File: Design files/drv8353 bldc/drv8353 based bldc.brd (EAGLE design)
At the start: 127 x 127 mm, 117 parts, among them IC1 DRV8353RSRGZT, J3 2X6 FEMALE, J4 B06B-HCMKK

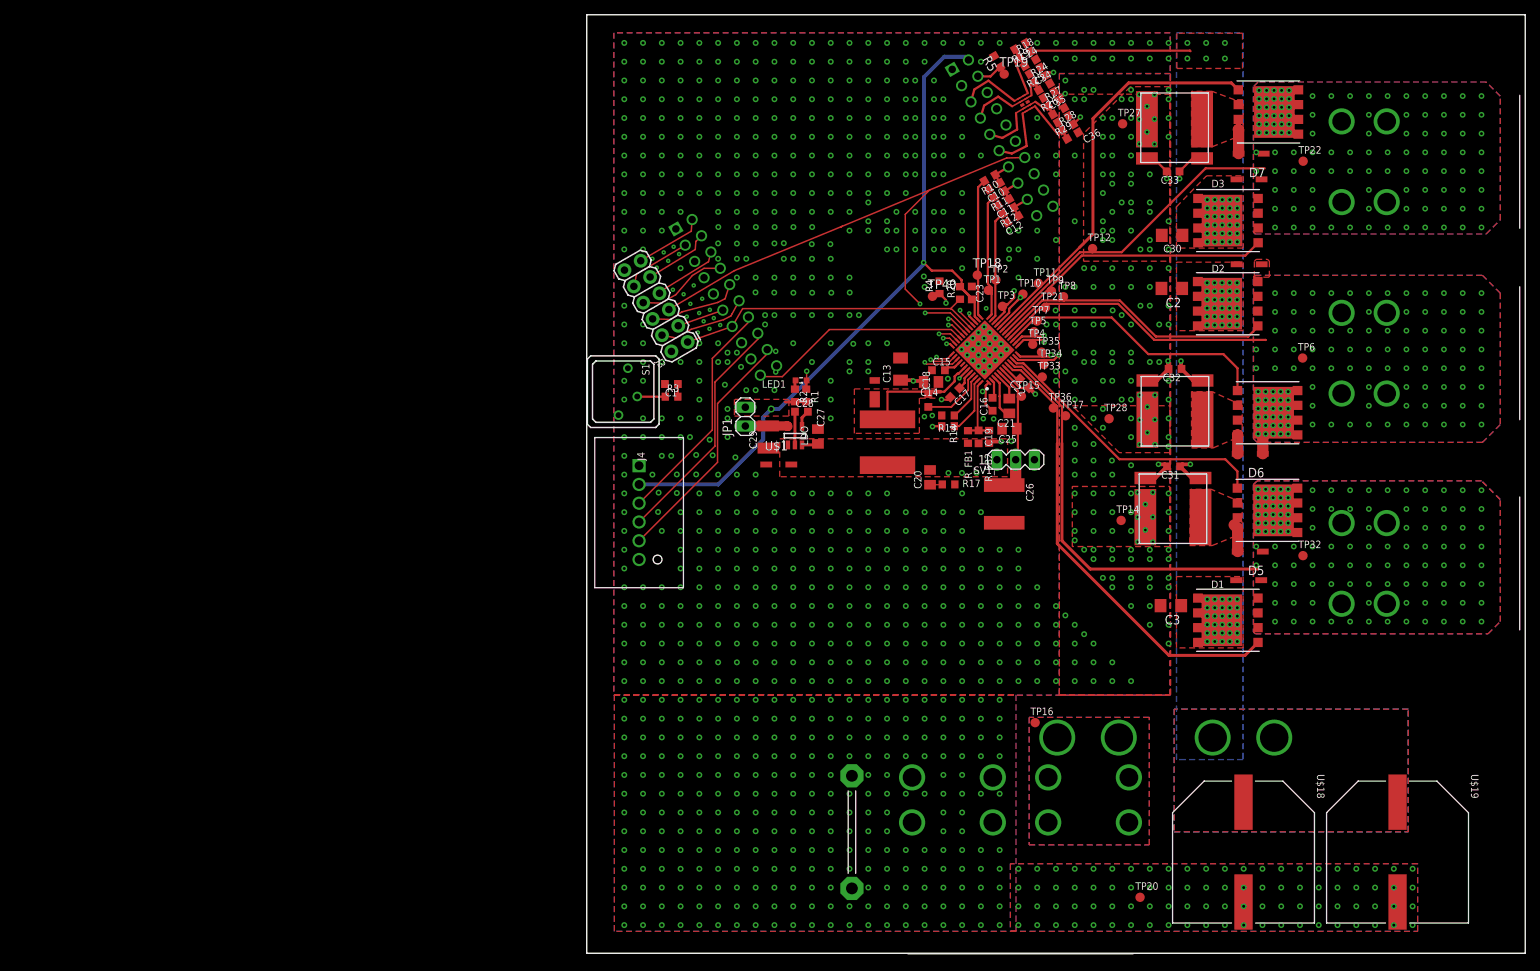
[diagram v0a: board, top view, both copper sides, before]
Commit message: silkscreen pass, slightly moved fuse to prevent part collision
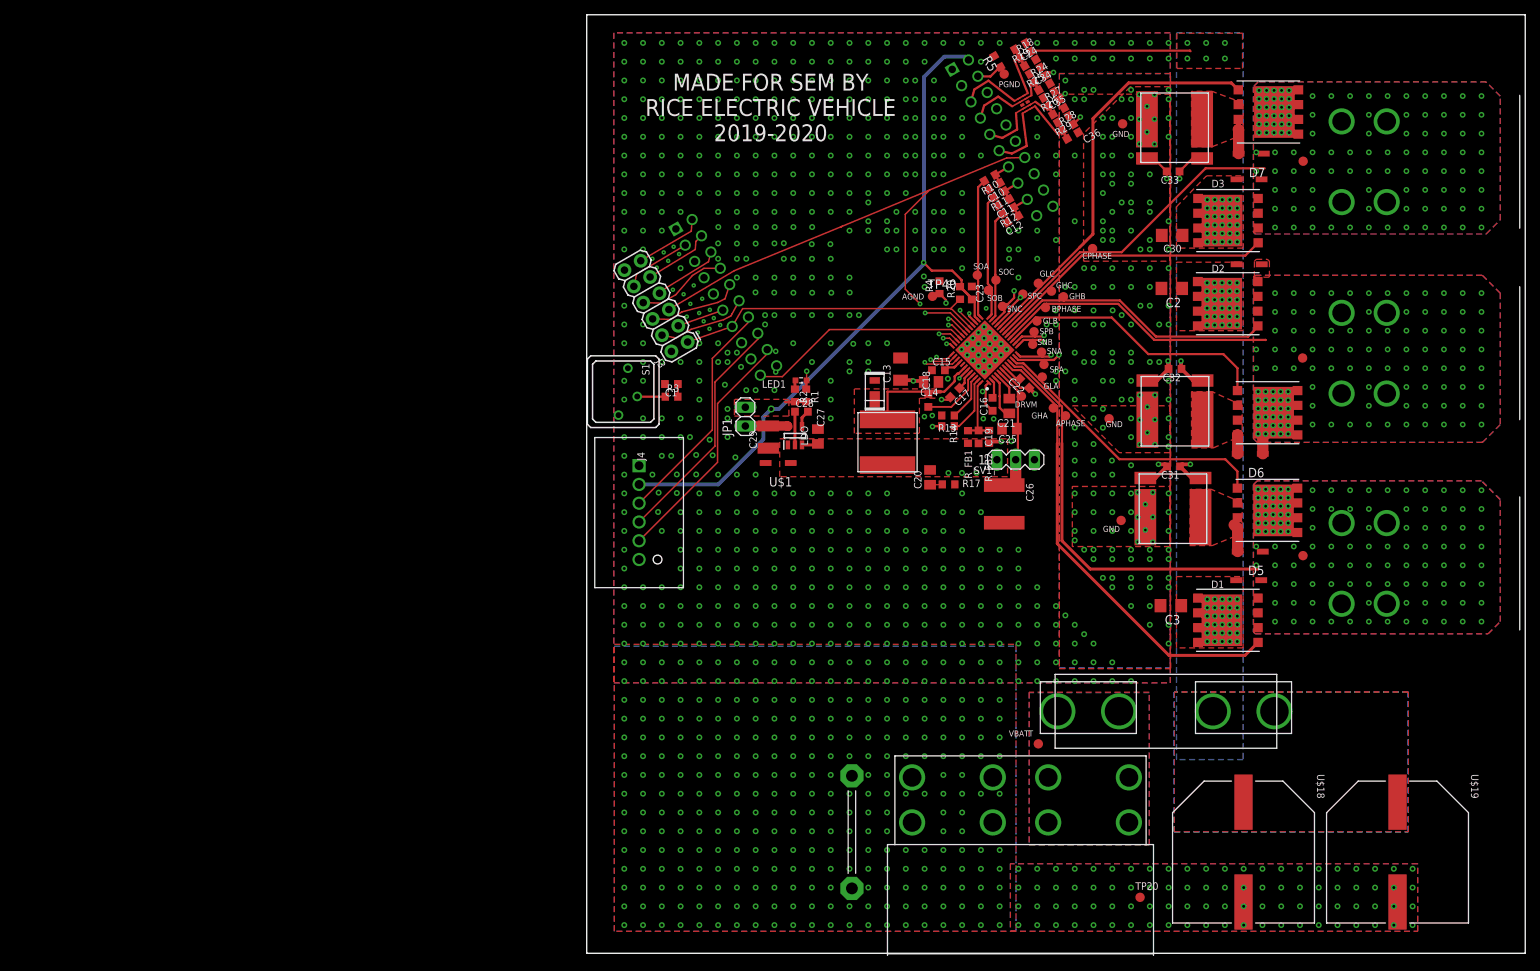
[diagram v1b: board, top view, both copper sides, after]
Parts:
- moved F1 3.56 mm to (78.4, 32.7)
- moved TP16 2.90 mm to (61.1, 28.3)
- moved U$1 0.22 mm to (25.9, 66.3), turned to 180 degrees
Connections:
- net APHASE: now also D5.LINE; no longer D5.1
- net BPHASE: now also D6.LINE; no longer D6.1
- net CPHASE: now also D7.LINE; no longer D7.1
- net GND: now also U$1.2; no longer U$1.1
- net VBUCK: now also U$1.LINE; no longer U$1.2
- net VDRAIN: now also D1.LINE, D2.LINE, D3.LINE; no longer D1.1, D2.1, D3.1
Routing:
- net VDRAIN: track 81.2 -> 78.2 mm
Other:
- board text added: "AGND"
- board text added: "APHASE"
- board text added: "BPHASE"
- board text added: "CPHASE"
- board text added: "DRVM"
- board text added: "GHA"
- board text added: "GHB"
- board text added: "GHC"
- board text added: "GLA"
- board text added: "GLB"
- board text added: "GLC"
- board text added: "GND"
- board text added: "MADE FOR SEM BY RICE ELECTRIC VEHICLE 2019-2020"
- board text added: "PGND"
- board text added: "SNA"
- board text added: "SNB"
- board text added: "SNC"
- board text added: "SOA"
- board text added: "SOB"
- board text added: "SOC"
- board text added: "SPA"
- board text added: "SPB"
- board text added: "SPC"
- board text added: "VBATT"

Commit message: corrected drc
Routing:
- net CPHASE: vias 111 -> 110
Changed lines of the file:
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@@
 <setting verticaltext="up"/>
 </settings>
-<grid distance="1" unitdist="mil" unit="mil" style="lines" multiple="1" display="no" altdistance="0.1" altunitdist="mil" altunit="mil"/>
+<grid distance="1" unitdist="mil" unit="mm" style="lines" multiple="1" display="no" altdistance="0.1" altunitdist="mil" altunit="mil"/>
 <layers>
 <layer number="1" name="Top" color="4" fill="1" visible="yes" active="yes"/>
@@
 <param name="mtCopper" value="0.035mm 0.0175mm 0.035mm 0.035mm 0.035mm 0.035mm 0.035mm 0.035mm 0.035mm 0.035mm 0.035mm 0.035mm 0.035mm 0.035mm 0.0175mm 0.035mm"/>
 <param name="mtIsolate" value="0.1mm 0.5mm 0.2mm 0.15mm 0.2mm 0.15mm 0.2mm 0.15mm 0.2mm 0.15mm 0.2mm 0.15mm 0.2mm 0.15mm 0.1mm"/>
-<param name="mdWireWire" value="6mil"/>
-<param name="mdWirePad" value="6mil"/>
-<param name="mdWireVia" value="6mil"/>
-<param name="mdPadPad" value="6mil"/>
-<param name="mdPadVia" value="6mil"/>
-<param name="mdViaVia" value="6mil"/>
+<param name="mdWireWire" value="0.2mm"/>
+<param name="mdWirePad" value="0.2mm"/>
+<param name="mdWireVia" value="0.2mm"/>
+<param name="mdPadPad" value="0.2mm"/>
+<param name="mdPadVia" value="0.2mm"/>
+<param name="mdViaVia" value="0.2mm"/>
 <param name="mdSmdPad" value="6mil"/>
 <param name="mdSmdVia" value="6mil"/>
@@
 <param name="mdDrill" value="6mil"/>
 <param name="mdSmdStop" value="0mil"/>
-<param name="msWidth" value="6mil"/>
-<param name="msDrill" value="10mil"/>
+<param name="msWidth" value="0.2mm"/>
+<param name="msDrill" value="0.2mm"/>
 <param name="msMicroVia" value="9.99mm"/>
 <param name="msBlindViaRatio" value="0.5"/>
@@
 <param name="rvMicroViaOuter" value="0.25"/>
 <param name="rvMicroViaInner" value="0.25"/>
-<param name="rlMinPadTop" value="10mil"/>
+<param name="rlMinPadTop" value="0.2mm"/>
 <param name="rlMaxPadTop" value="20mil"/>
-<param name="rlMinPadInner" value="10mil"/>
+<param name="rlMinPadInner" value="0.2mm"/>
 <param name="rlMaxPadInner" value="20mil"/>
-<param name="rlMinPadBottom" value="10mil"/>
+<param name="rlMinPadBottom" value="0.2mm"/>
 <param name="rlMaxPadBottom" value="20mil"/>
-<param name="rlMinViaOuter" value="8mil"/>
+<param name="rlMinViaOuter" value="0.2mm"/>
 <param name="rlMaxViaOuter" value="20mil"/>
-<param name="rlMinViaInner" value="8mil"/>
+<param name="rlMinViaInner" value="0.2mm"/>
 <param name="rlMaxViaInner" value="20mil"/>
 <param name="rlMinMicroViaOuter" value="4mil"/>
@@
 <wire x1="28.1758" y1="73.2824" x2="28.1796" y2="73.2862" width="0.4064" layer="1"/>
 <wire x1="24.5636" y1="68.3582" x2="24.6398" y2="68.3582" width="0.508" layer="1"/>
+<wire x1="51.4858" y1="80.9498" x2="50.86859375" y2="79.69425625" width="0" layer="19" extent="1-1"/>
+<wire x1="59.6695625" y1="115.21495" x2="60.96" y2="113.03" width="0" layer="19" extent="1-1"/>
+<wire x1="55.662825" y1="101.1909" x2="56.897225" y2="98.9091" width="0" layer="19" extent="1-1"/>
+<wire x1="54.408025" y1="103.3795" x2="55.662825" y2="101.1909" width="0" layer="19" extent="1-1"/>
 </signal>
 <signal name="SNA">
@@
 <contactref element="IC1" pad="44"/>
 <contactref element="C17" pad="2"/>
-<wire x1="50.450021875" y1="76.47998125" x2="50.450021875" y2="76.951159375" width="0.3048" layer="1"/>
+<wire x1="50.450021875" y1="76.47998125" x2="50.450021875" y2="76.925759375" width="0.3048" layer="1"/>
 <wire x1="51.92925625" y1="78.63359375" x2="51.1302" y2="77.8345375" width="0.3048" layer="1"/>
 <wire x1="51.1302" y1="77.8345375" x2="51.1302" y2="77.1652" width="0.3048" layer="1"/>
@@
 <vertex x="26.1138" y="69.620875"/>
 <vertex x="56.9484" y="69.615428125"/>
-<vertex x="56.9484" y="69.615428125"/>
 <vertex x="56.9484" y="64.486"/>
 </polygon>
@@
 <via x="93.1418" y="100.7618" extent="1-16" drill="0.381"/>
 <via x="93.1418" y="98.2218" extent="1-16" drill="0.381"/>
-<via x="90.6018" y="108.3818" extent="1-16" drill="0.381"/>
 <via x="90.6018" y="105.8418" extent="1-16" drill="0.381"/>
 <polygon width="0.1524" layer="2">

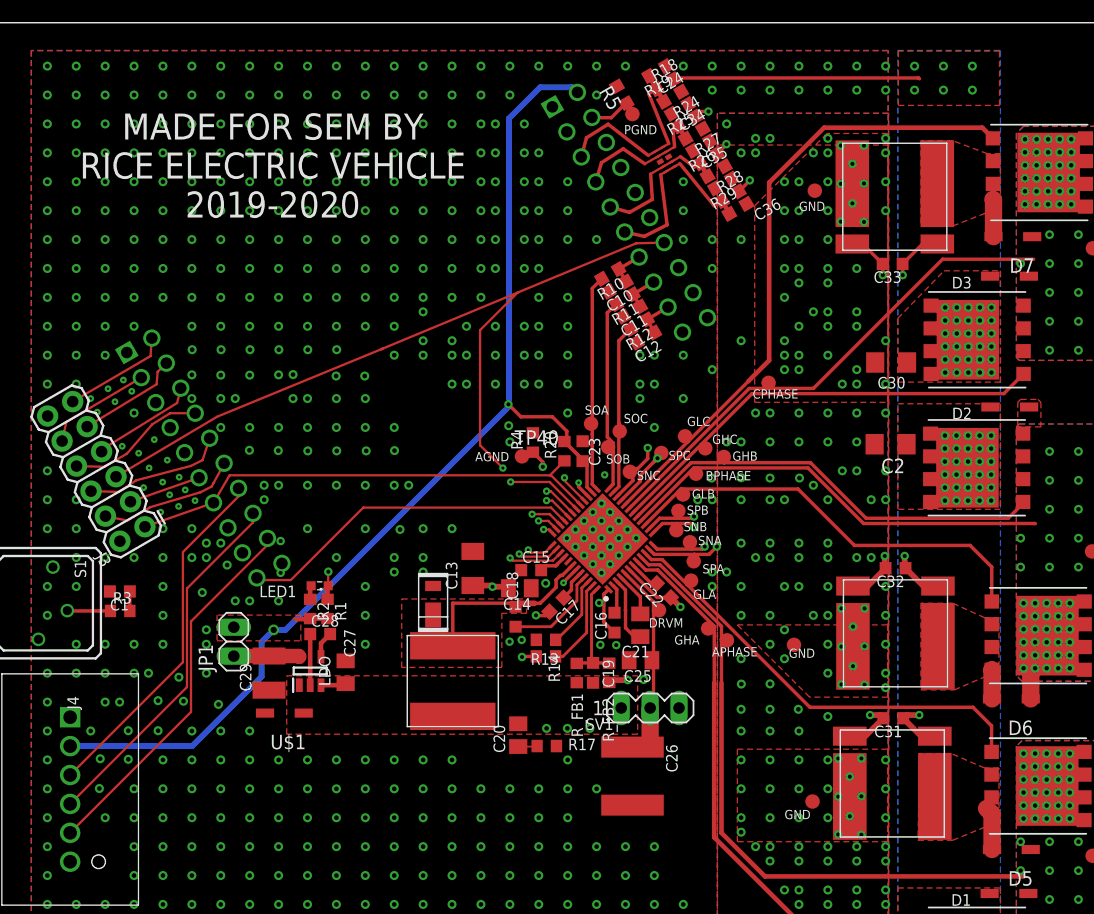
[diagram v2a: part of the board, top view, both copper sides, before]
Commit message: fixed board for jlpcb 2oz service
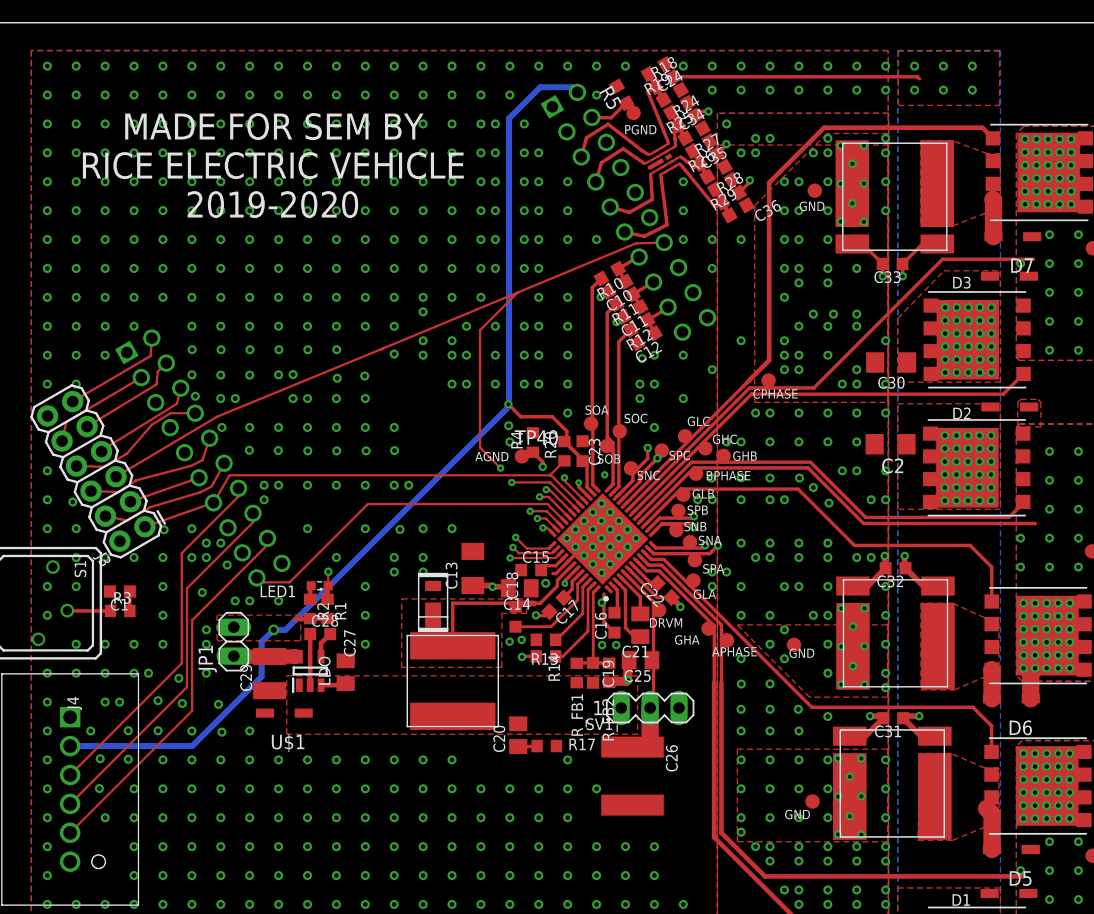
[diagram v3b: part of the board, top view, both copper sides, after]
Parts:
- moved TP3 0.32 mm to (56.4, 87.8)
- moved TP10 0.22 mm to (59.1, 89.4)
- moved TP33 0.20 mm to (61.8, 78.0)
- moved TP12 0.20 mm to (68.5, 95.6)
- moved R18 0.18 mm to (59.3, 121.8)
- moved R19 0.18 mm to (58.6, 122.9)
- moved C24 0.16 mm to (60.0, 120.7)
- moved TP34 0.14 mm to (62.0, 79.8)
- moved TP1 0.14 mm to (54.3, 89.8)
- moved TP19 0.14 mm to (56.6, 119.1)
- moved C36 0.14 mm to (65.8, 110.5)
- moved R28 0.13 mm to (65.1, 111.6)
- moved R25 0.12 mm to (60.6, 119.5)
- moved R29 0.10 mm to (64.5, 112.8)
- moved TP8 0.09 mm to (64.5, 88.9)
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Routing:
- net GND: track 12.5 -> 19.4 mm, vias 1185 -> 1161
- net SPC: track 41.1 -> 42.9 mm
- net DRV_VM: track 17.1 -> 18.8 mm
- net VSENA: track 12.7 -> 14.1 mm
- net SNB: track 28.0 -> 29.4 mm
- net VSENC: track 17.3 -> 18.7 mm
- net VSENB: track 12.9 -> 14.2 mm
- net NFAULT: track 45.5 -> 46.4 mm
- net GLB: track 38.7 -> 39.3 mm
- net GHC: track 39.9 -> 40.4 mm
- net GLA: track 39.8 -> 40.3 mm
- net APHASE: vias 116 -> 115

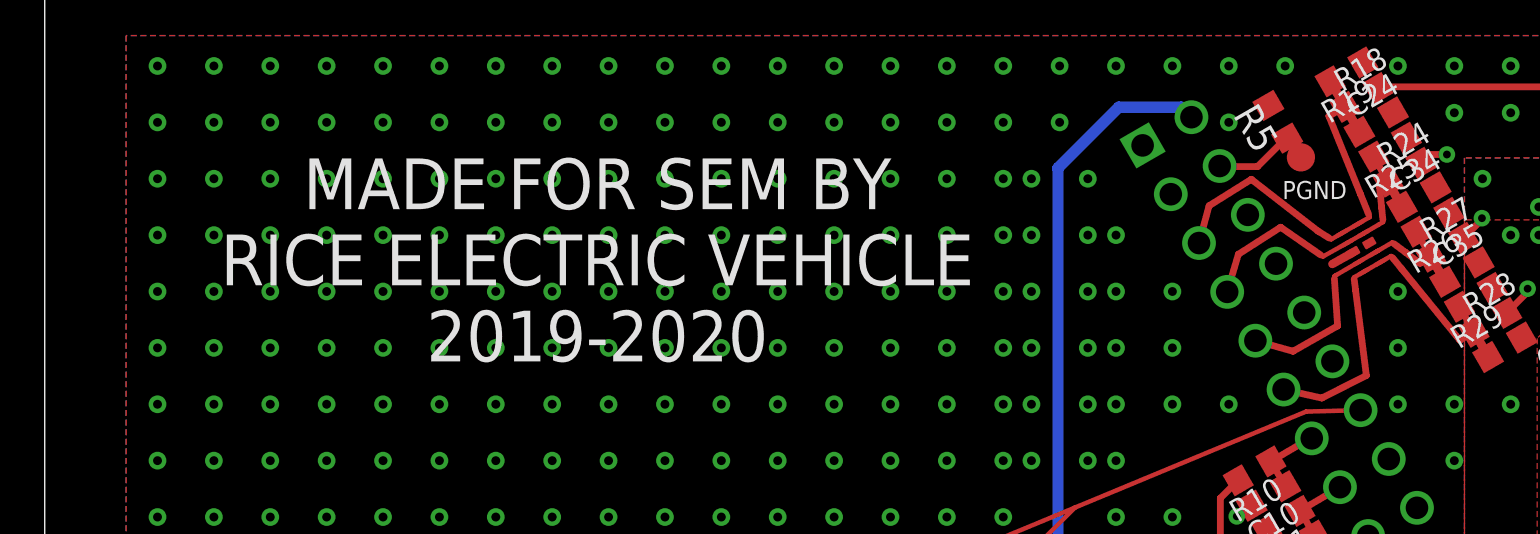
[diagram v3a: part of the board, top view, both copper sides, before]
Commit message: moves VSENA away from ADC B; got rid of some vias by the text
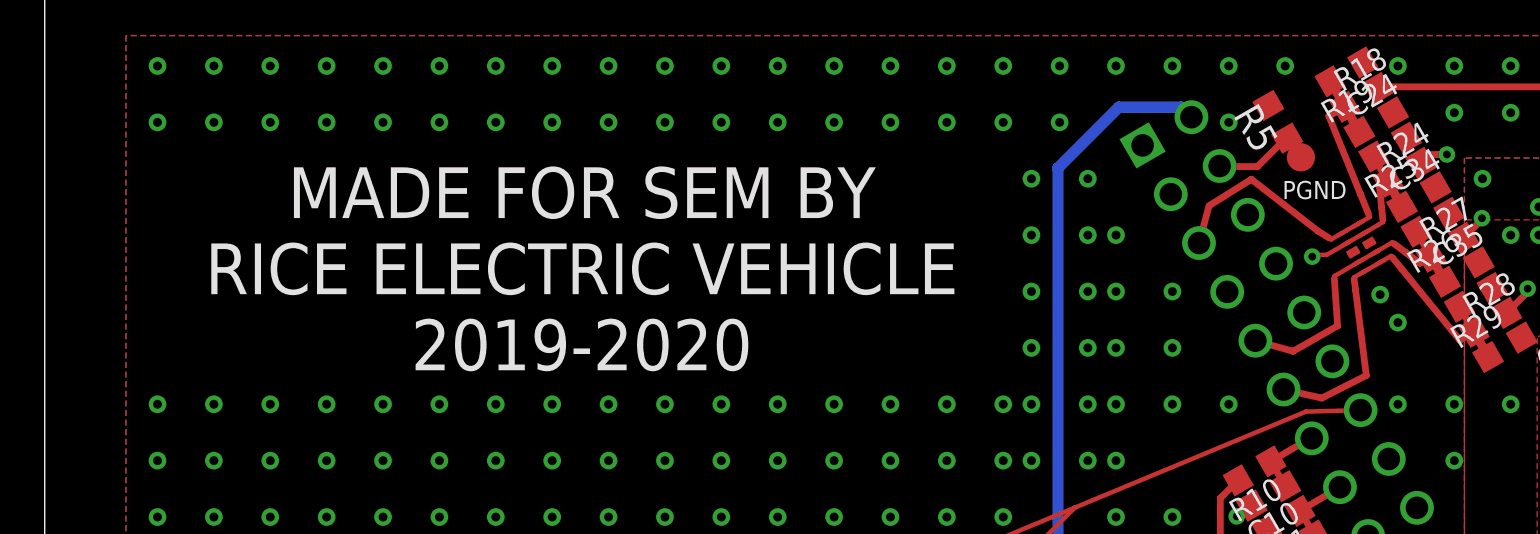
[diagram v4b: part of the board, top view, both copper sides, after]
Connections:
- net VSENA: now also U$2.30; no longer U$2.24
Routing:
- net VSENA: track 14.1 -> 25.1 mm, vias 0 -> 1
- net GND: track 19.4 -> 18.3 mm, vias 1161 -> 1097
